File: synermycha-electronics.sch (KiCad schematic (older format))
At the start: 0 parts

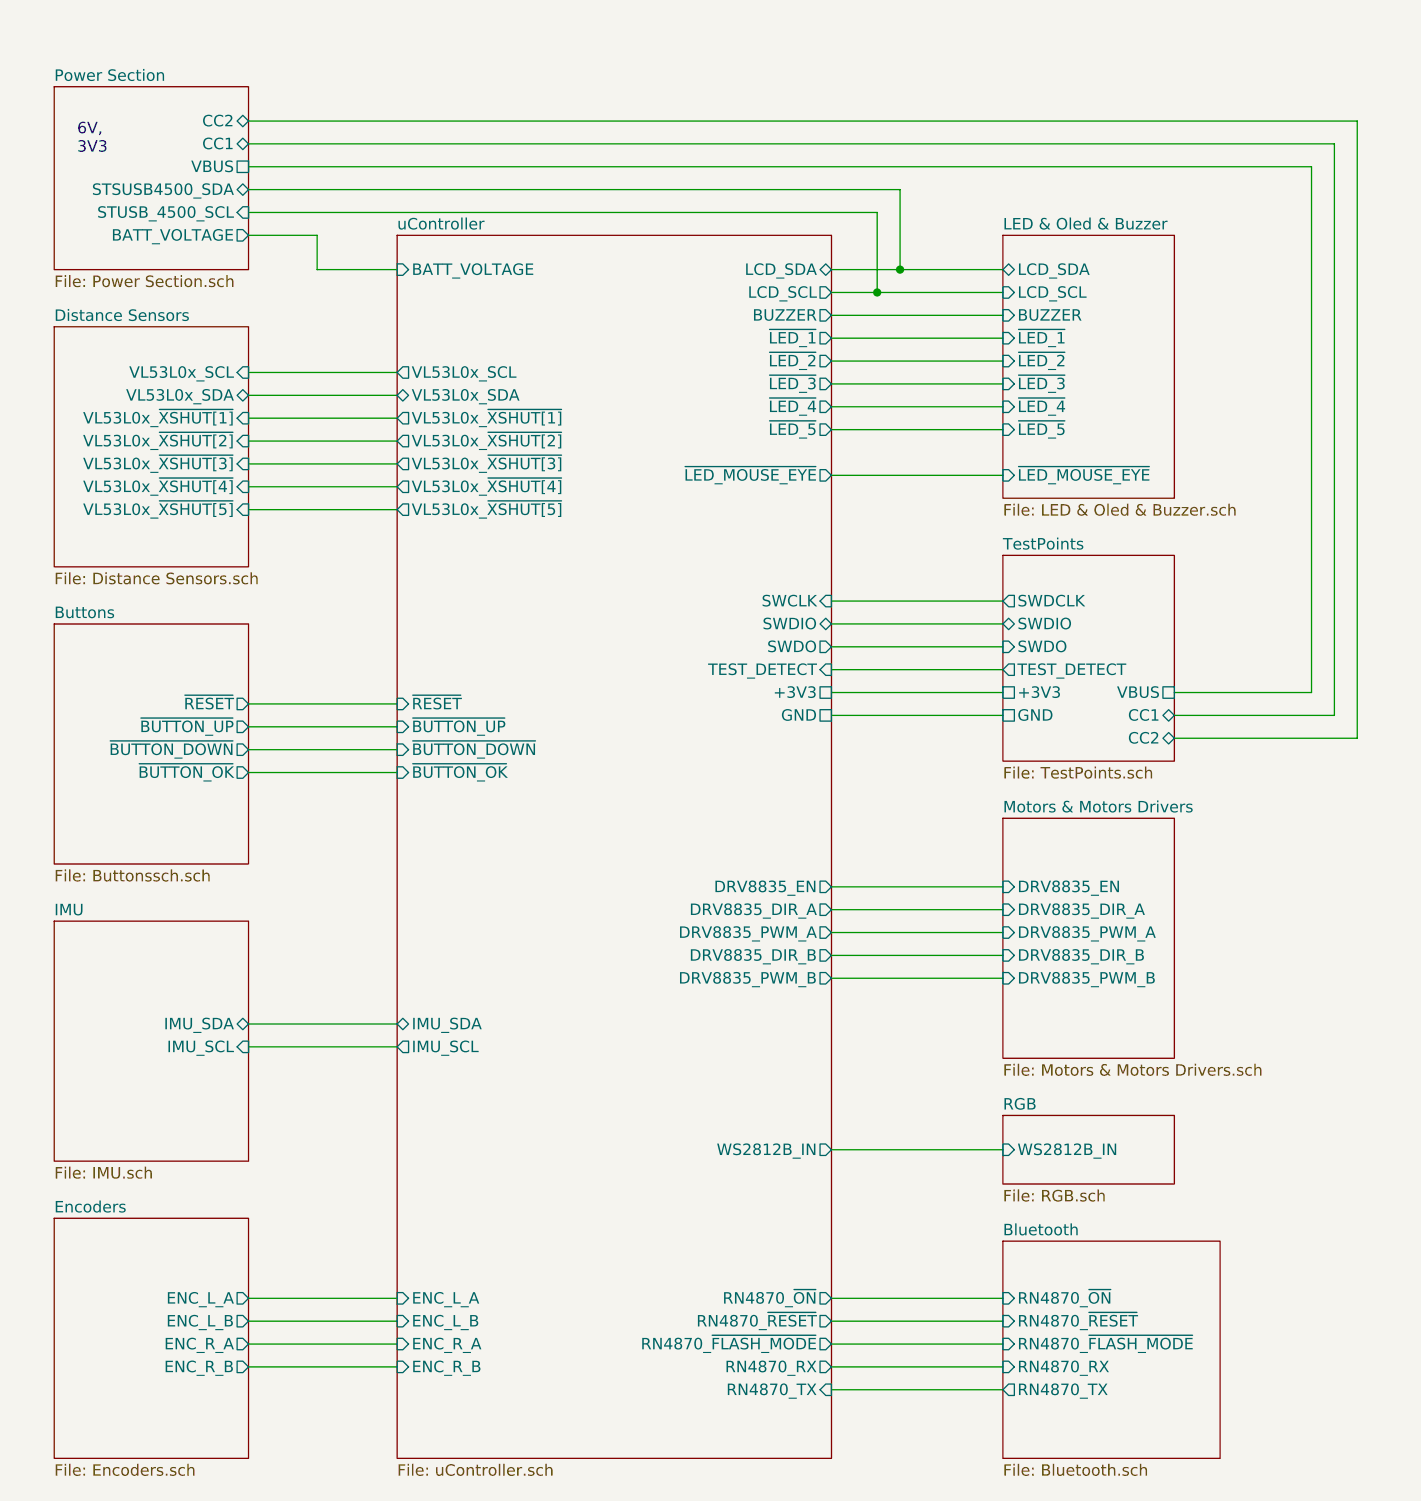
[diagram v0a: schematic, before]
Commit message: Dodano ścieżki łączące STM do USB
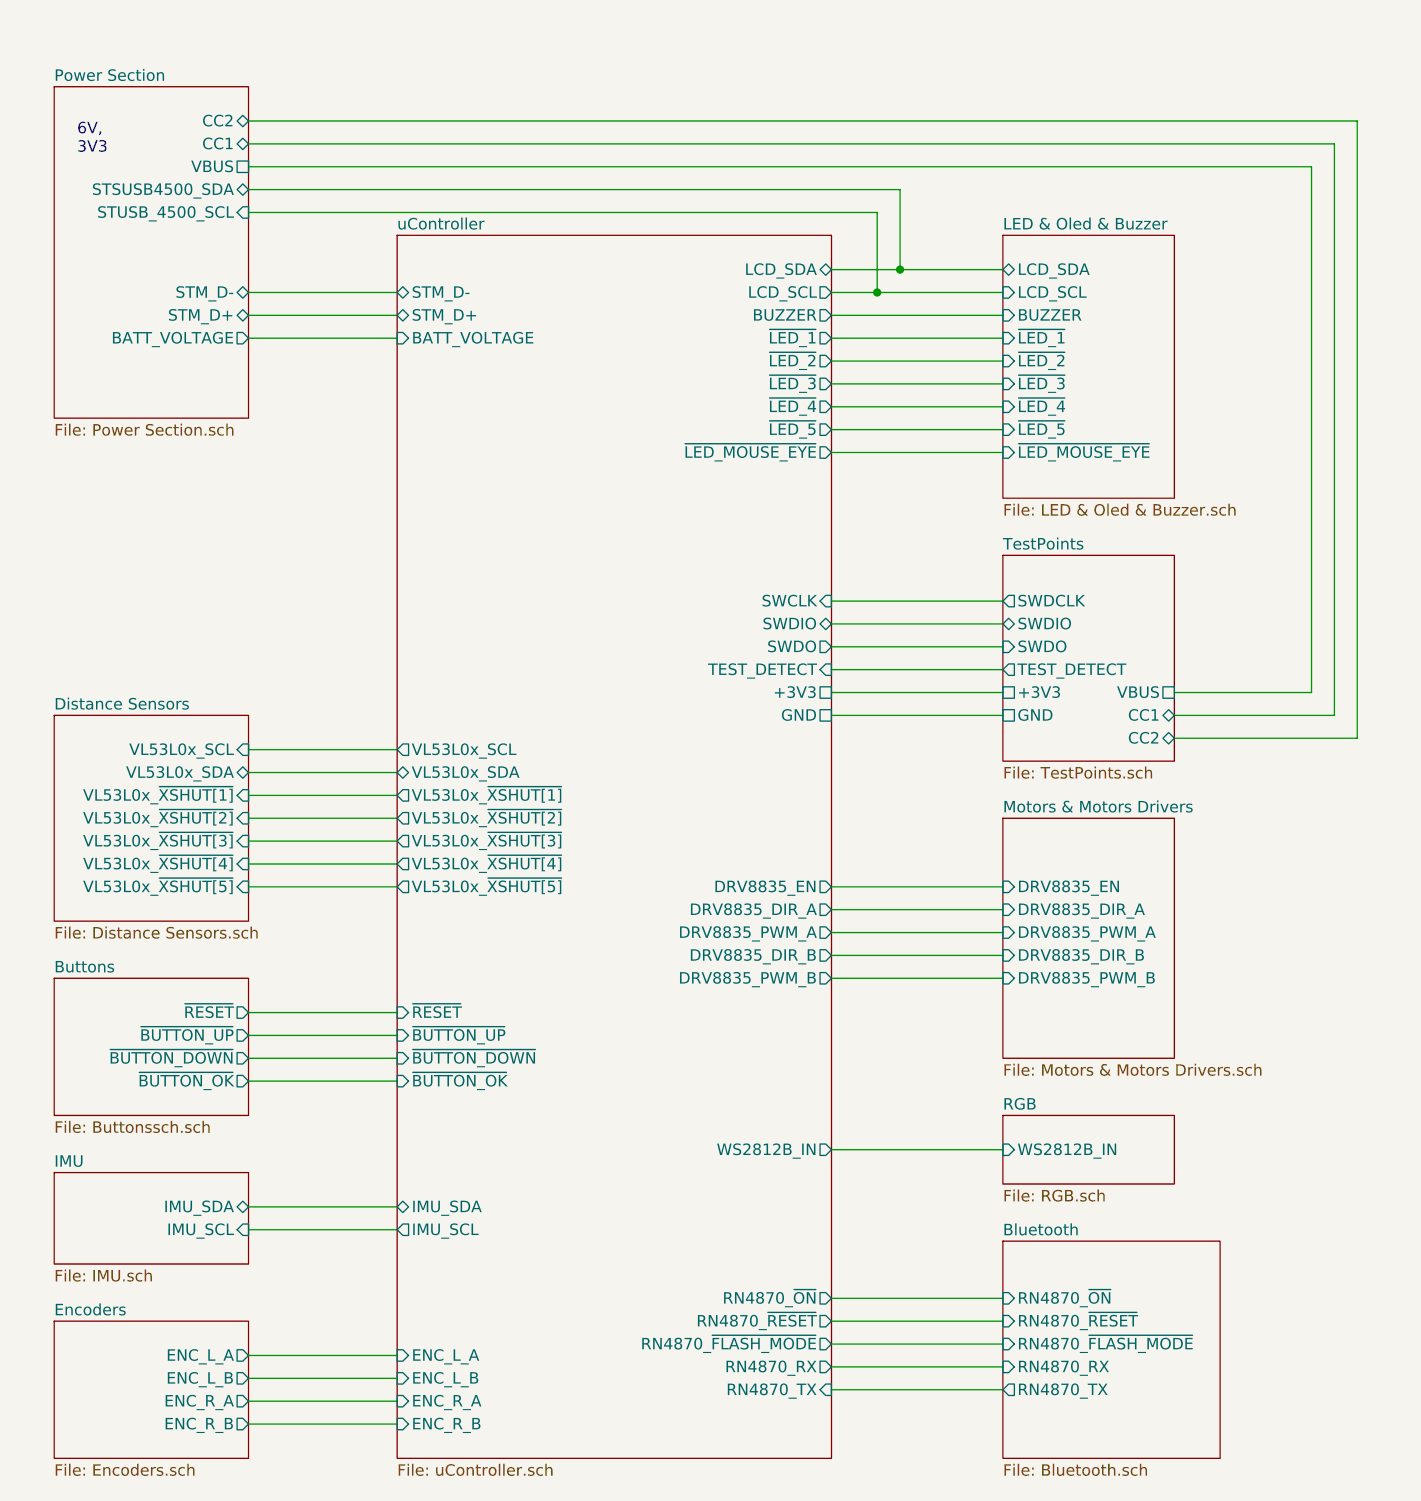
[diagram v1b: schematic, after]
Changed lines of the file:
@@
 $EndSheet
 $Sheet
-S 1350 4650 850  1050
+S 1350 6200 850  600
 U 5E5F55F9
 F0 "Buttons" 50
 F1 "Buttonssch.sch" 50
-F2 "~RESET" O R 2200 5000 50
-F3 "~BUTTON_UP" O R 2200 5100 50
-F4 "~BUTTON_DOWN" O R 2200 5200 50
-F5 "~BUTTON_OK" O R 2200 5300 50
-$EndSheet
-$Sheet
-S 1350 3350 850  1050
+F2 "~RESET" O R 2200 6350 50
+F3 "~BUTTON_UP" O R 2200 6450 50
+F4 "~BUTTON_DOWN" O R 2200 6550 50
+F5 "~BUTTON_OK" O R 2200 6650 50
+$EndSheet
+$Sheet
+S 1350 5050 850  900
 U 5E5F5567
 F0 "Distance Sensors" 50
 F1 "Distance Sensors.sch" 50
-F2 "VL53L0x_SCL" I R 2200 3550 50
-F3 "VL53L0x_SDA" B R 2200 3650 50
-F4 "VL53L0x_~XSHUT[1]" I R 2200 3750 50
-F5 "VL53L0x_~XSHUT[2]" I R 2200 3850 50
-F6 "VL53L0x_~XSHUT[3]" I R 2200 3950 50
-F7 "VL53L0x_~XSHUT[4]" I R 2200 4050 50
-F8 "VL53L0x_~XSHUT[5]" I R 2200 4150 50
+F2 "VL53L0x_SCL" I R 2200 5200 50
+F3 "VL53L0x_SDA" B R 2200 5300 50
+F4 "VL53L0x_~XSHUT[1]" I R 2200 5400 50
+F5 "VL53L0x_~XSHUT[2]" I R 2200 5500 50
+F6 "VL53L0x_~XSHUT[3]" I R 2200 5600 50
+F7 "VL53L0x_~XSHUT[4]" I R 2200 5700 50
+F8 "VL53L0x_~XSHUT[5]" I R 2200 5800 50
 $EndSheet
 Text Notes 1450 2600 0    50   ~ 0
 6V,\n3V3\n
 $Sheet
-S 1350 7250 850  1050
-U 5E5F5610
-F0 "Encoders" 50
-F1 "Encoders.sch" 50
-F2 "ENC_L_A" O R 2200 7600 50
-F3 "ENC_L_B" O R 2200 7700 50
-F4 "ENC_R_A" O R 2200 7800 50
-F5 "ENC_R_B" O R 2200 7900 50
-$EndSheet
-$Sheet
-S 1350 5950 850  1050
+S 1350 7050 850  400
 U 5E6F1BD7
 F0 "IMU" 50
 F1 "IMU.sch" 50
-F2 "IMU_SDA" B R 2200 6400 50
-F3 "IMU_SCL" I R 2200 6500 50
-$EndSheet
-Wire Wire Line
-	2200 5000 2850 5000
-Wire Wire Line
-	2200 5100 2850 5100
-Wire Wire Line
-	2850 5200 2200 5200
-Wire Wire Line
-	2200 5300 2850 5300
-Wire Wire Line
-	2200 6400 2850 6400
-Wire Wire Line
-	2850 6500 2200 6500
-Wire Wire Line
-	2200 7600 2850 7600
-Wire Wire Line
-	2850 7700 2200 7700
-Wire Wire Line
-	2200 7800 2850 7800
-Wire Wire Line
-	2850 7900 2200 7900
+F2 "IMU_SDA" B R 2200 7200 50
+F3 "IMU_SCL" I R 2200 7300 50
+$EndSheet
+Wire Wire Line
+	2200 6350 2850 6350
+Wire Wire Line
+	2200 6450 2850 6450
+Wire Wire Line
+	2850 6550 2200 6550
+Wire Wire Line
+	2200 6650 2850 6650
+Wire Wire Line
+	2200 7200 2850 7200
+Wire Wire Line
+	2850 7300 2200 7300
+Wire Wire Line
+	2200 7850 2850 7850
+Wire Wire Line
+	2850 7950 2200 7950
+Wire Wire Line
+	2200 8050 2850 8050
+Wire Wire Line
+	2850 8150 2200 8150
 Wire Wire Line
 	5500 7900 4750 7900
@@
 	5500 8000 4750 8000
 Wire Wire Line
-	2200 3550 2850 3550
-Wire Wire Line
-	2850 3650 2200 3650
-Wire Wire Line
-	2200 3750 2850 3750
-Wire Wire Line
-	2850 3850 2200 3850
-Wire Wire Line
-	2200 3950 2850 3950
+	2200 5200 2850 5200
+Wire Wire Line
+	2850 5300 2200 5300
+Wire Wire Line
+	2200 5400 2850 5400
+Wire Wire Line
+	2850 5500 2200 5500
+Wire Wire Line
+	2200 5600 2850 5600
 $Sheet
 S 2850 2950 1900 5350
@@
 F0 "uController" 50
 F1 "uController.sch" 50
-F2 "~RESET" I L 2850 5000 50
-F3 "~BUTTON_UP" I L 2850 5100 50
-F4 "~BUTTON_DOWN" I L 2850 5200 50
-F5 "~BUTTON_OK" I L 2850 5300 50
-F6 "VL53L0x_SCL" O L 2850 3550 50
-F7 "VL53L0x_SDA" B L 2850 3650 50
-F8 "VL53L0x_~XSHUT[1]" O L 2850 3750 50
-F9 "VL53L0x_~XSHUT[2]" O L 2850 3850 50
-F10 "VL53L0x_~XSHUT[3]" O L 2850 3950 50
-F11 "ENC_L_A" I L 2850 7600 50
-F12 "ENC_L_B" I L 2850 7700 50
-F13 "ENC_R_A" I L 2850 7800 50
-F14 "ENC_R_B" I L 2850 7900 50
-F15 "IMU_SDA" B L 2850 6400 50
-F16 "IMU_SCL" O L 2850 6500 50
+F2 "~RESET" I L 2850 6350 50
+F3 "~BUTTON_UP" I L 2850 6450 50
+F4 "~BUTTON_DOWN" I L 2850 6550 50
+F5 "~BUTTON_OK" I L 2850 6650 50
+F6 "VL53L0x_SCL" O L 2850 5200 50
+F7 "VL53L0x_SDA" B L 2850 5300 50
+F8 "VL53L0x_~XSHUT[1]" O L 2850 5400 50
+F9 "VL53L0x_~XSHUT[2]" O L 2850 5500 50
+F10 "VL53L0x_~XSHUT[3]" O L 2850 5600 50
+F11 "ENC_L_A" I L 2850 7850 50
+F12 "ENC_L_B" I L 2850 7950 50
+F13 "ENC_R_A" I L 2850 8050 50
+F14 "ENC_R_B" I L 2850 8150 50
+F15 "IMU_SDA" B L 2850 7200 50
+F16 "IMU_SCL" O L 2850 7300 50
 F17 "RN4870_RX" O R 4750 7900 50
 F18 "RN4870_TX" I R 4750 8000 50
-F19 "BATT_VOLTAGE" I L 2850 3100 50
+F19 "BATT_VOLTAGE" I L 2850 3400 50
 F20 "LCD_SDA" B R 4750 3100 50
 F21 "LCD_SCL" O R 4750 3200 50
@@
 F26 "~LED_4" O R 4750 3700 50
 F27 "~LED_5" O R 4750 3800 50
-F28 "~LED_MOUSE_EYE" O R 4750 4000 50
+F28 "~LED_MOUSE_EYE" O R 4750 3900 50
 F29 "DRV8835_EN" O R 4750 5800 50
 F30 "DRV8835_DIR_A" O R 4750 5900 50
@@
 F32 "DRV8835_PWM_A" O R 4750 6000 50
 F33 "DRV8835_PWM_B" O R 4750 6200 50
-F34 "VL53L0x_~XSHUT[4]" O L 2850 4050 50
-F35 "VL53L0x_~XSHUT[5]" O L 2850 4150 50
+F34 "VL53L0x_~XSHUT[4]" O L 2850 5700 50
+F35 "VL53L0x_~XSHUT[5]" O L 2850 5800 50
 F36 "WS2812B_IN" O R 4750 6950 50
 F37 "RN4870_~ON" O R 4750 7600 50
@@
 F44 "+3V3" U R 4750 4950 50
 F45 "GND" U R 4750 5050 50
+F46 "STM_D+" B L 2850 3300 50
+F47 "STM_D-" B L 2850 3200 50
 $EndSheet
 Wire Wire Line
@@
 F8 "~LED_4" I L 5500 3700 50
 F9 "~LED_5" I L 5500 3800 50
-F10 "~LED_MOUSE_EYE" I L 5500 4000 50
-$EndSheet
-Wire Wire Line
-	2200 4050 2850 4050
-Wire Wire Line
-	2850 4150 2200 4150
-Wire Wire Line
-	4750 4000 5500 4000
+F10 "~LED_MOUSE_EYE" I L 5500 3900 50
+$EndSheet
+Wire Wire Line
+	2200 5700 2850 5700
+Wire Wire Line
+	2850 5800 2200 5800
+Wire Wire Line
+	4750 3900 5500 3900
 $Sheet
 S 5500 6800 750  300
@@
 	4750 4950 5500 4950
 Wire Wire Line
-	2850 3100 2500 3100
-Wire Wire Line
-	2500 3100 2500 2950
-Wire Wire Line
-	2500 2950 2200 2950
-Wire Wire Line
 	2200 2850 4950 2850
 Wire Wire Line
@@
 	2200 2650 6850 2650
 $Sheet
-S 1350 2300 850  800
+S 1350 2300 850  1450
 U 5E5F54DF
 F0 "Power Section" 50
 F1 "Power Section.sch" 50
-F2 "BATT_VOLTAGE" O R 2200 2950 50
+F2 "BATT_VOLTAGE" O R 2200 3400 50
 F3 "STSUSB4500_SDA" B R 2200 2750 50
 F4 "STUSB_4500_SCL" I R 2200 2850 50
@@
 F6 "CC1" B R 2200 2550 50
 F7 "CC2" B R 2200 2450 50
+F8 "STM_D-" B R 2200 3200 50
+F9 "STM_D+" B R 2200 3300 50
 $EndSheet
 Wire Wire Line
@@
 Wire Wire Line
 	7050 5150 6250 5150
+$Sheet
+S 1350 7700 850  600
+U 5E5F5610
+F0 "Encoders" 50
+F1 "Encoders.sch" 50
+F2 "ENC_L_A" O R 2200 7850 50
+F3 "ENC_L_B" O R 2200 7950 50
+F4 "ENC_R_A" O R 2200 8050 50
+F5 "ENC_R_B" O R 2200 8150 50
+$EndSheet
+Wire Wire Line
+	2200 3400 2850 3400
+Wire Wire Line
+	2850 3300 2200 3300
+Wire Wire Line
+	2850 3200 2200 3200
 $EndSCHEMATC

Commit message: Dodano projekt stacji dokującej. Poprawki ścieżek i shcematu
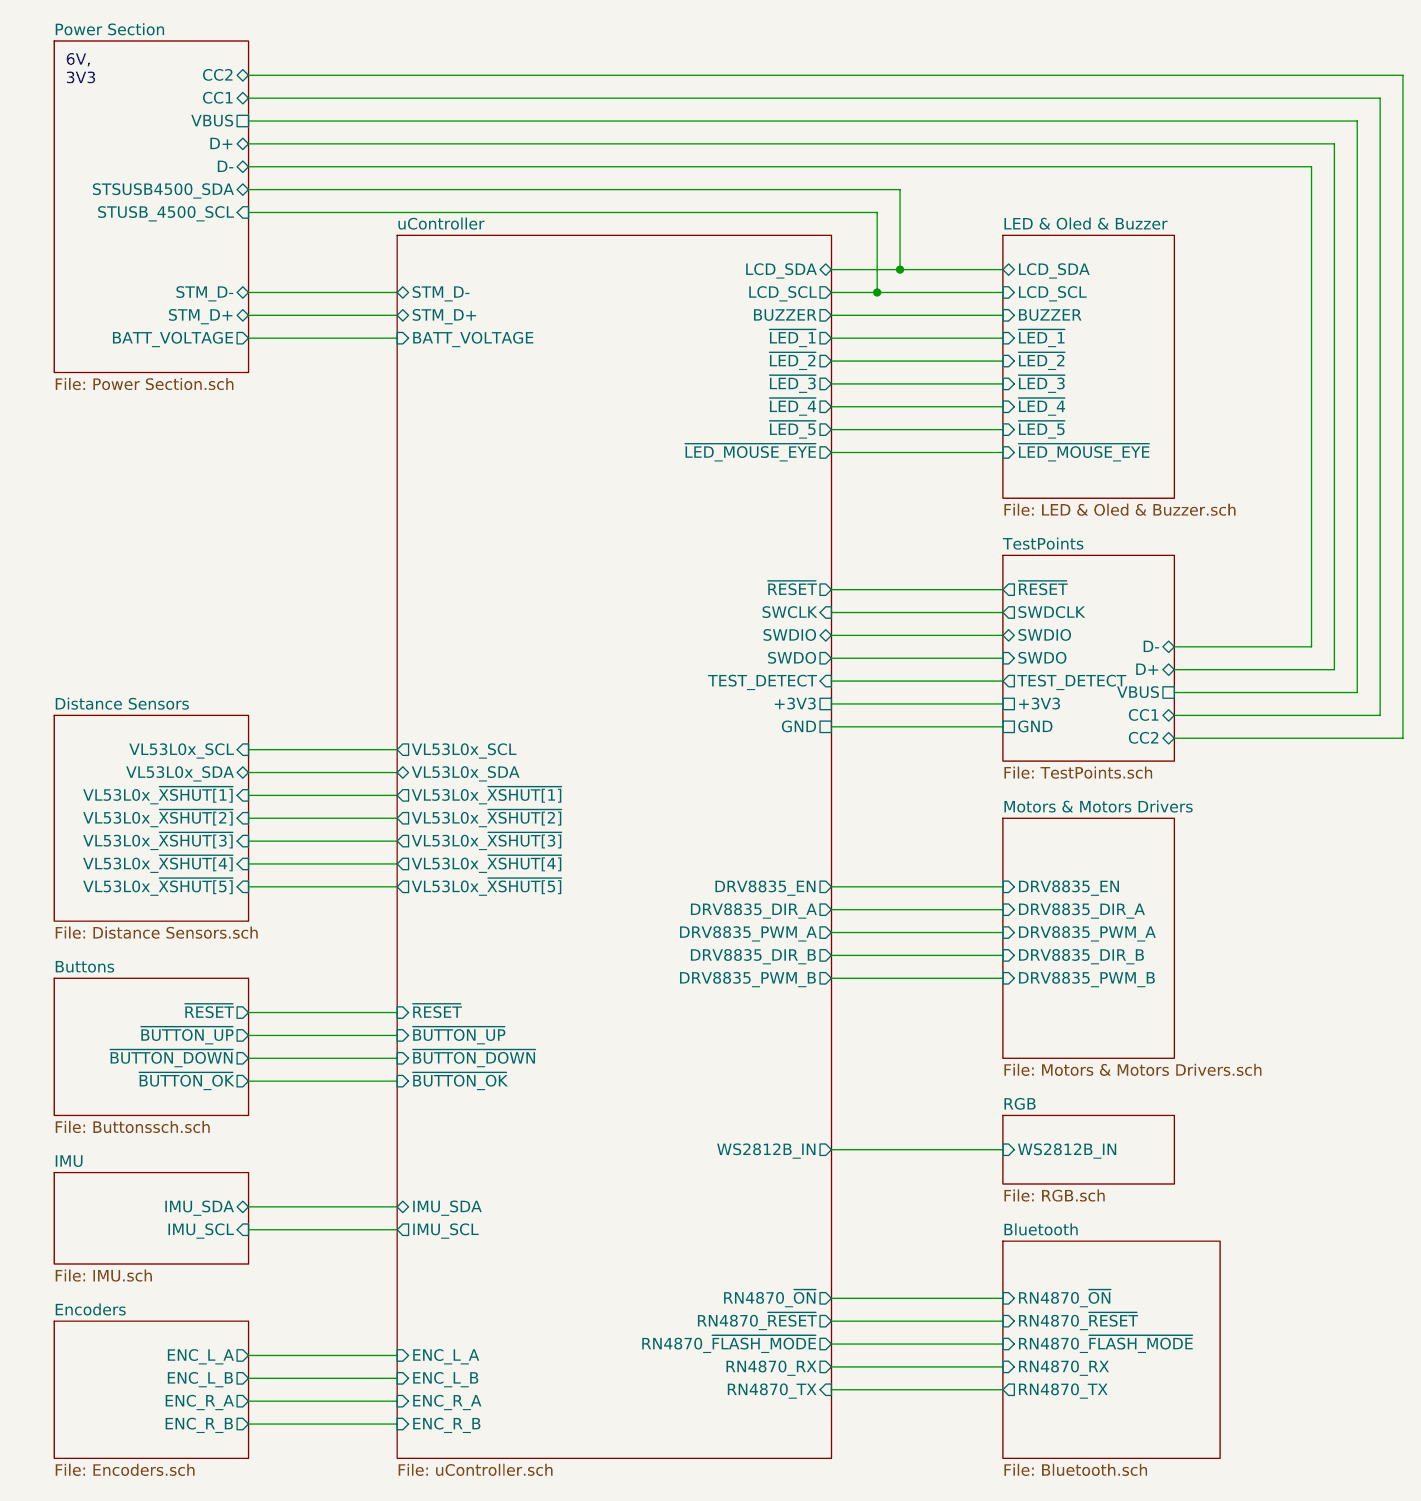
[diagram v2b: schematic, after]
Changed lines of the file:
@@
 F8 "VL53L0x_~XSHUT[5]" I R 2200 5800 50
 $EndSheet
-Text Notes 1450 2600 0    50   ~ 0
+Text Notes 1400 2300 0    50   ~ 0
 6V,\n3V3\n
 $Sheet
@@
 F38 "RN4870_~RESET" O R 4750 7700 50
 F39 "RN4870_~FLASH_MODE" O R 4750 7800 50
-F40 "SWCLK" I R 4750 4550 50
-F41 "SWDIO" B R 4750 4650 50
-F42 "SWDO" O R 4750 4750 50
-F43 "TEST_DETECT" I R 4750 4850 50
-F44 "+3V3" U R 4750 4950 50
-F45 "GND" U R 4750 5050 50
+F40 "SWCLK" I R 4750 4600 50
+F41 "SWDIO" B R 4750 4700 50
+F42 "SWDO" O R 4750 4800 50
+F43 "TEST_DETECT" I R 4750 4900 50
+F44 "+3V3" U R 4750 5000 50
+F45 "GND" U R 4750 5100 50
 F46 "STM_D+" B L 2850 3300 50
 F47 "STM_D-" B L 2850 3200 50
+F48 "~RESET" O R 4750 4500 50
 $EndSheet
 Wire Wire Line
@@
 F0 "TestPoints" 50
 F1 "TestPoints.sch" 50
-F2 "SWDCLK" O L 5500 4550 50
-F3 "SWDIO" B L 5500 4650 50
-F4 "SWDO" I L 5500 4750 50
-F5 "TEST_DETECT" O L 5500 4850 50
-F6 "+3V3" U L 5500 4950 50
-F7 "GND" U L 5500 5050 50
+F2 "SWDCLK" O L 5500 4600 50
+F3 "SWDIO" B L 5500 4700 50
+F4 "SWDO" I L 5500 4800 50
+F5 "TEST_DETECT" O L 5500 4900 50
+F6 "+3V3" U L 5500 5000 50
+F7 "GND" U L 5500 5100 50
 F8 "VBUS" U R 6250 4950 50
 F9 "CC1" B R 6250 5050 50
 F10 "CC2" B R 6250 5150 50
-$EndSheet
-Wire Wire Line
-	4750 4550 5500 4550
-Wire Wire Line
-	4750 4650 5500 4650
-Wire Wire Line
-	4750 4750 5500 4750
-Wire Wire Line
-	4750 4850 5500 4850
-Wire Wire Line
-	4750 5050 5500 5050
-Wire Wire Line
-	4750 4950 5500 4950
+F11 "~RESET" O L 5500 4500 50
+F12 "D+" B R 6250 4850 50
+F13 "D-" B R 6250 4750 50
+$EndSheet
+Wire Wire Line
+	4750 4600 5500 4600
+Wire Wire Line
+	4750 4700 5500 4700
+Wire Wire Line
+	4750 4800 5500 4800
+Wire Wire Line
+	4750 4900 5500 4900
+Wire Wire Line
+	4750 5100 5500 5100
+Wire Wire Line
+	4750 5000 5500 5000
 Wire Wire Line
 	2200 2850 4950 2850
@@
 Wire Wire Line
 	2200 2650 6850 2650
-$Sheet
-S 1350 2300 850  1450
-U 5E5F54DF
-F0 "Power Section" 50
-F1 "Power Section.sch" 50
-F2 "BATT_VOLTAGE" O R 2200 3400 50
-F3 "STSUSB4500_SDA" B R 2200 2750 50
-F4 "STUSB_4500_SCL" I R 2200 2850 50
-F5 "VBUS" U R 2200 2650 50
-F6 "CC1" B R 2200 2550 50
-F7 "CC2" B R 2200 2450 50
-F8 "STM_D-" B R 2200 3200 50
-F9 "STM_D+" B R 2200 3300 50
-$EndSheet
-Wire Wire Line
-	6250 4950 6850 4950
-Wire Wire Line
-	6850 2650 6850 4950
+Wire Wire Line
+	6850 2650 6850 4750
 Wire Wire Line
 	2200 2550 6950 2550
 Wire Wire Line
-	6950 2550 6950 5050
-Wire Wire Line
-	6950 5050 6250 5050
+	6950 2550 6950 4850
 Wire Wire Line
 	2200 2450 7050 2450
-Wire Wire Line
-	7050 2450 7050 5150
-Wire Wire Line
-	7050 5150 6250 5150
 $Sheet
 S 1350 7700 850  600
@@
 Wire Wire Line
 	2850 3200 2200 3200
+Wire Wire Line
+	4750 4500 5500 4500
+$Sheet
+S 1350 2100 850  1450
+U 5E5F54DF
+F0 "Power Section" 50
+F1 "Power Section.sch" 50
+F2 "BATT_VOLTAGE" O R 2200 3400 50
+F3 "STSUSB4500_SDA" B R 2200 2750 50
+F4 "STUSB_4500_SCL" I R 2200 2850 50
+F5 "VBUS" U R 2200 2450 50
+F6 "CC1" B R 2200 2350 50
+F7 "CC2" B R 2200 2250 50
+F8 "STM_D-" B R 2200 3200 50
+F9 "STM_D+" B R 2200 3300 50
+F10 "D-" B R 2200 2650 50
+F11 "D+" B R 2200 2550 50
+$EndSheet
+Wire Wire Line
+	6250 4750 6850 4750
+Wire Wire Line
+	6250 4850 6950 4850
+Wire Wire Line
+	6250 4950 7050 4950
+Wire Wire Line
+	7050 4950 7050 2450
+Wire Wire Line
+	7150 5050 7150 2350
+Wire Wire Line
+	7150 2350 2200 2350
+Wire Wire Line
+	6250 5050 7150 5050
+Wire Wire Line
+	7250 5150 7250 2250
+Wire Wire Line
+	7250 2250 2200 2250
+Wire Wire Line
+	6250 5150 7250 5150
 $EndSCHEMATC
